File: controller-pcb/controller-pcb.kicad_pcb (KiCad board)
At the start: 2 copper layers, 94.8 x 24.5 mm, 11 parts, among them J1 24V_IN1, J2 24V_IN2, J3 LED1 (IO6), J4 LED2 (IO7), U1 ESP32-C3_SUPERMINI_SMD, U2 5V_DCDC

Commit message: v1
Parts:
- removed the REF** at (88.5, 86.2)
- removed the REF** at (88.5, 67.5)
- removed the REF** at (142.0, 67.5)
- added J5: MIC, LEDnet:INMP441_Breakout, F.Cu at (104.2, 86.2)
- D1: footprint Diode_THT:D_DO-41_SOD81_P10.16mm_Horizontal -> Diode_THT:D_DO-41_SOD81_P7.62mm_Horizontal
- J1: value 24V_IN1 -> 24V; footprint Connector_BarrelJack:BarrelJack_Horizontal -> LEDnet:BarrelJack_Horizontal_Trimmed
- J2: value 24V_IN2 -> 24V; footprint Connector_BarrelJack:BarrelJack_Horizontal -> LEDnet:BarrelJack_Horizontal_Trimmed
- J3: renamed from J4; value LED2 (IO7) -> LED1
- J4: renamed from J3; value LED1 (IO6) -> LED2
- U2: renamed from U1; value ESP32-C3_SUPERMINI_SMD -> ESP32
- moved REF** 25.5 mm to (118.2, 76.7)
- moved U2 20.2 mm to (134.5, 76.1)
- moved D1 19.3 mm to (122.8, 80.6)
- moved U1 9.68 mm to (99.5, 75.0)
- moved J3 9.46 mm to (120.0, 69.5), turned to 180 degrees
- moved J4 9.46 mm to (120.0, 84.0), turned to 180 degrees
- moved J1 2.75 mm to (81.0, 69.6)
- moved J2 2.75 mm to (81.0, 81.8)
- renumbered U2 to U1
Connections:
- J3 pad 2: Net-(J4-DATA_OUT) -> /LED1_DATA
- J4 pad 2: Net-(J3-DATA_OUT) -> /LED2_DATA
- U2 pad 10: unconnected-(U1-GPIO10-Pad10) -> /MIC_SD
- U2 pad 3: unconnected-(U1-GPIO3-Pad3) -> /LED1_DATA
- U2 pad 3.3: unconnected-(U1-3V3-Pad3.3) -> +3V3
- U2 pad 4: unconnected-(U1-GPIO4-Pad4) -> /LED2_DATA
- U2 pad 5: unconnected-(U1-GPIO5-Pad5) -> /MIC_SCK
- U2 pad 6: Net-(J3-DATA_OUT) -> unconnected-(U2-GPIO6-Pad6)
- U2 pad 7: Net-(J4-DATA_OUT) -> /MIC_WS
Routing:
- net /MIC_SD: track 0.00 -> 40.0 mm, vias 0 -> 1
- net /MIC_WS: track 0.00 -> 37.8 mm, vias 0 -> 1
- net /MIC_SCK: track 0.00 -> 37.4 mm, vias 0 -> 1
- net +3V3: track 0.00 -> 34.7 mm
- net /LED1_DATA: track 0.00 -> 12.0 mm, vias 0 -> 2
- net /LED2_DATA: track 0.00 -> 11.4 mm
- net Net-(D1-K): track 0.00 -> 11.0 mm, vias 0 -> 1
- net +5V: track 0.00 -> 5.52 mm
- net VCC: track 1.50 -> 0.00 mm, vias 0 -> 6
- net GND: vias 0 -> 46
- added copper zone on B.Cu, net VCC
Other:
- board size 94.8 x 24.5 mm -> 74.5 x 24.5 mm
- board text added: "Driver v1"

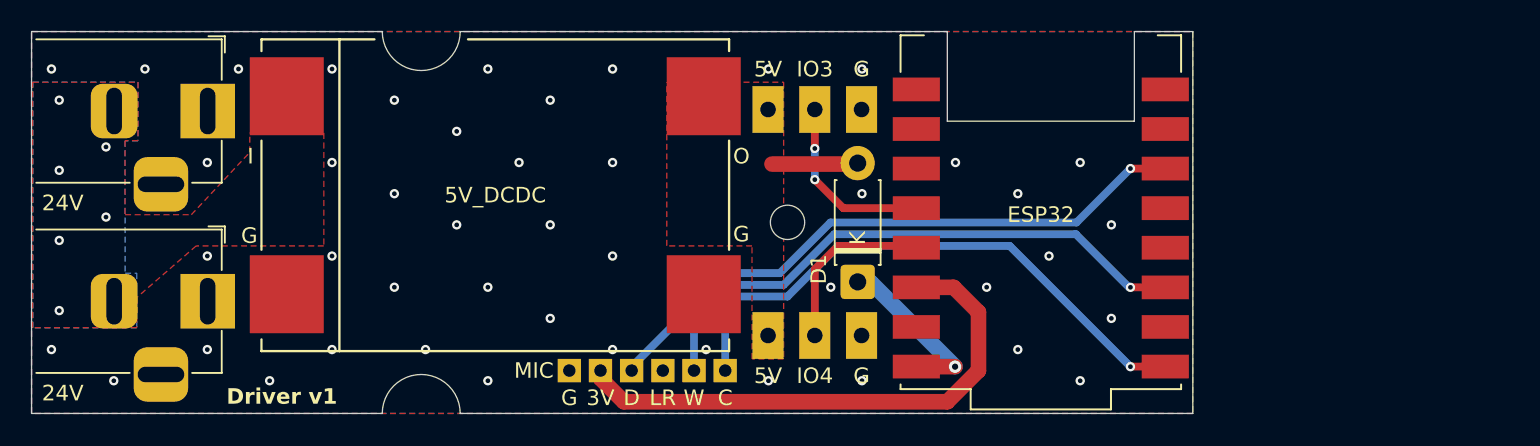
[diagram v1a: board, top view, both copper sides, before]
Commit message: fix dc jack polarity
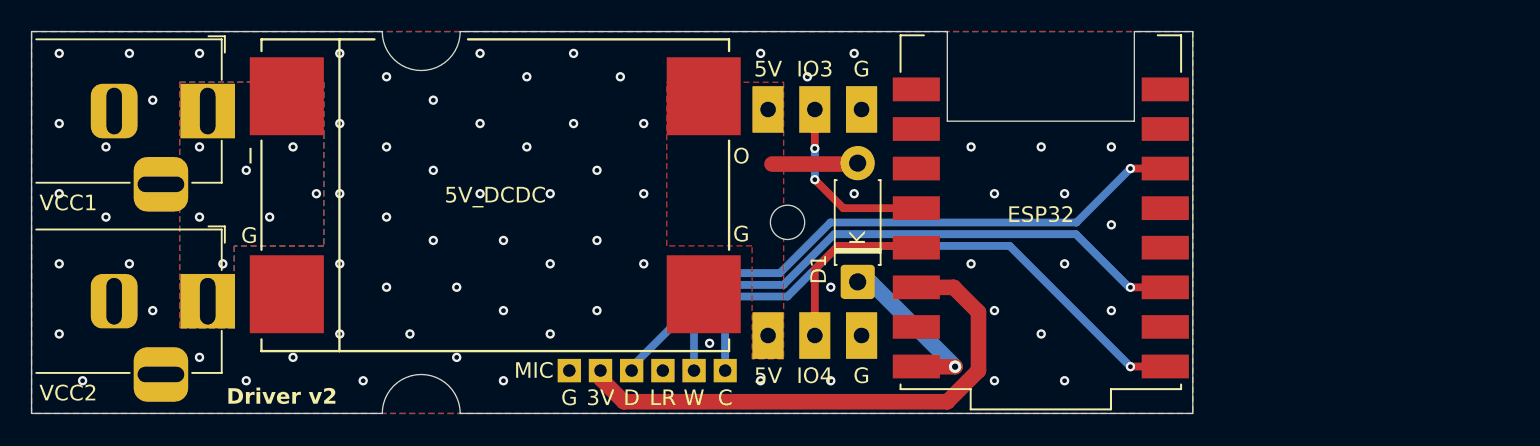
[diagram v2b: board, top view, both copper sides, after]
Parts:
- J1: value 24V -> VCC1
- J2: value 24V -> VCC2
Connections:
- J1 pad 1: GND -> VCC
- J1 pad 2: VCC -> GND
- J2 pad 1: GND -> VCC
- J2 pad 2: VCC -> GND
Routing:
- net VCC: vias 6 -> 7
- net GND: vias 46 -> 73
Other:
- board text added: "Driver v2"
- board text removed: "Driver v1"
